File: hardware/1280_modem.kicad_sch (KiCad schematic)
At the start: 84 parts, among them IC1 SX1281IMLTRT, IC2 SKY65383-11, IC3 TJA1462AT_0Z, J2 Conn_Coaxial, J2 jst gh 4, J5 jst gh 6, J8 USB_C_Receptacle_USB2.0, J9 jst_sh 6, U13 STM32U575CGTx, U2 TPS7A20285PDBVR, U2 USBLC6-2SC6, U4 TPS7A2450DBVR, Y1 48MHz, Y1 52MHz

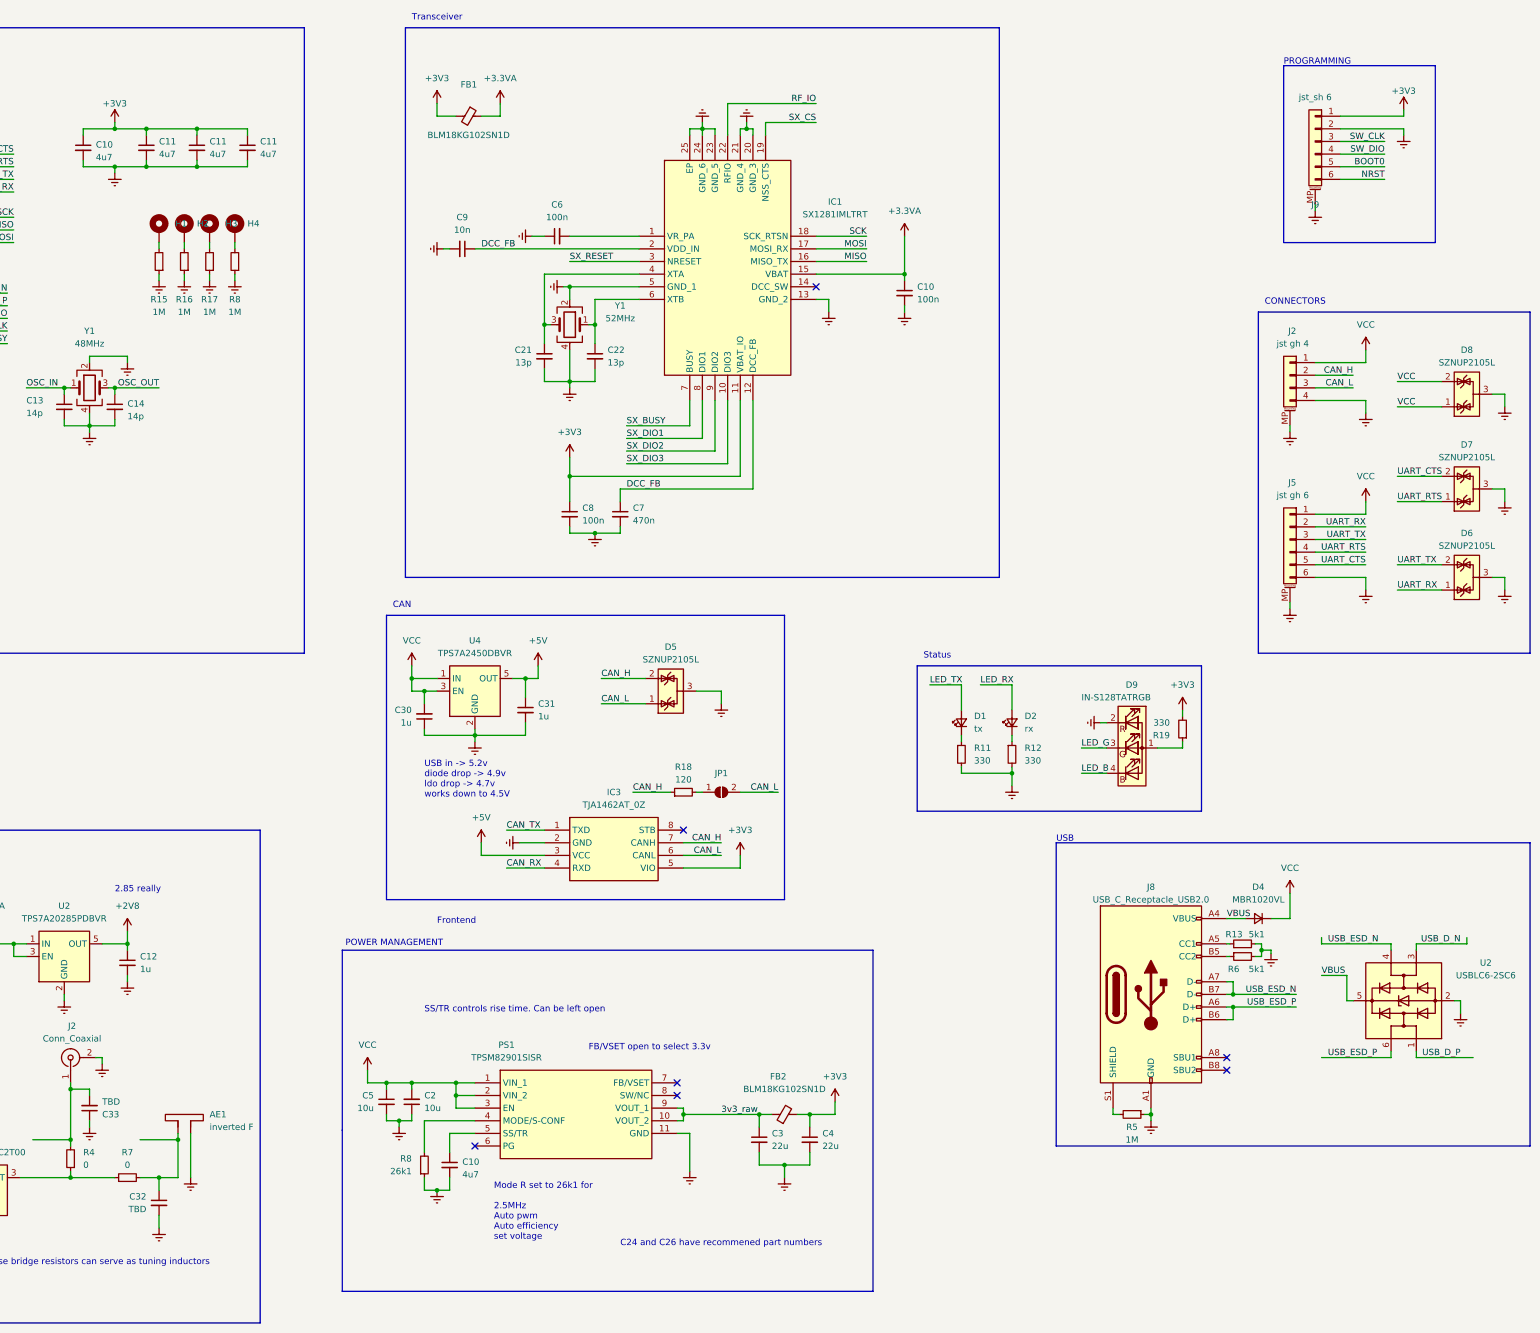
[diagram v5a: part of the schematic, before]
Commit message: better power electronics
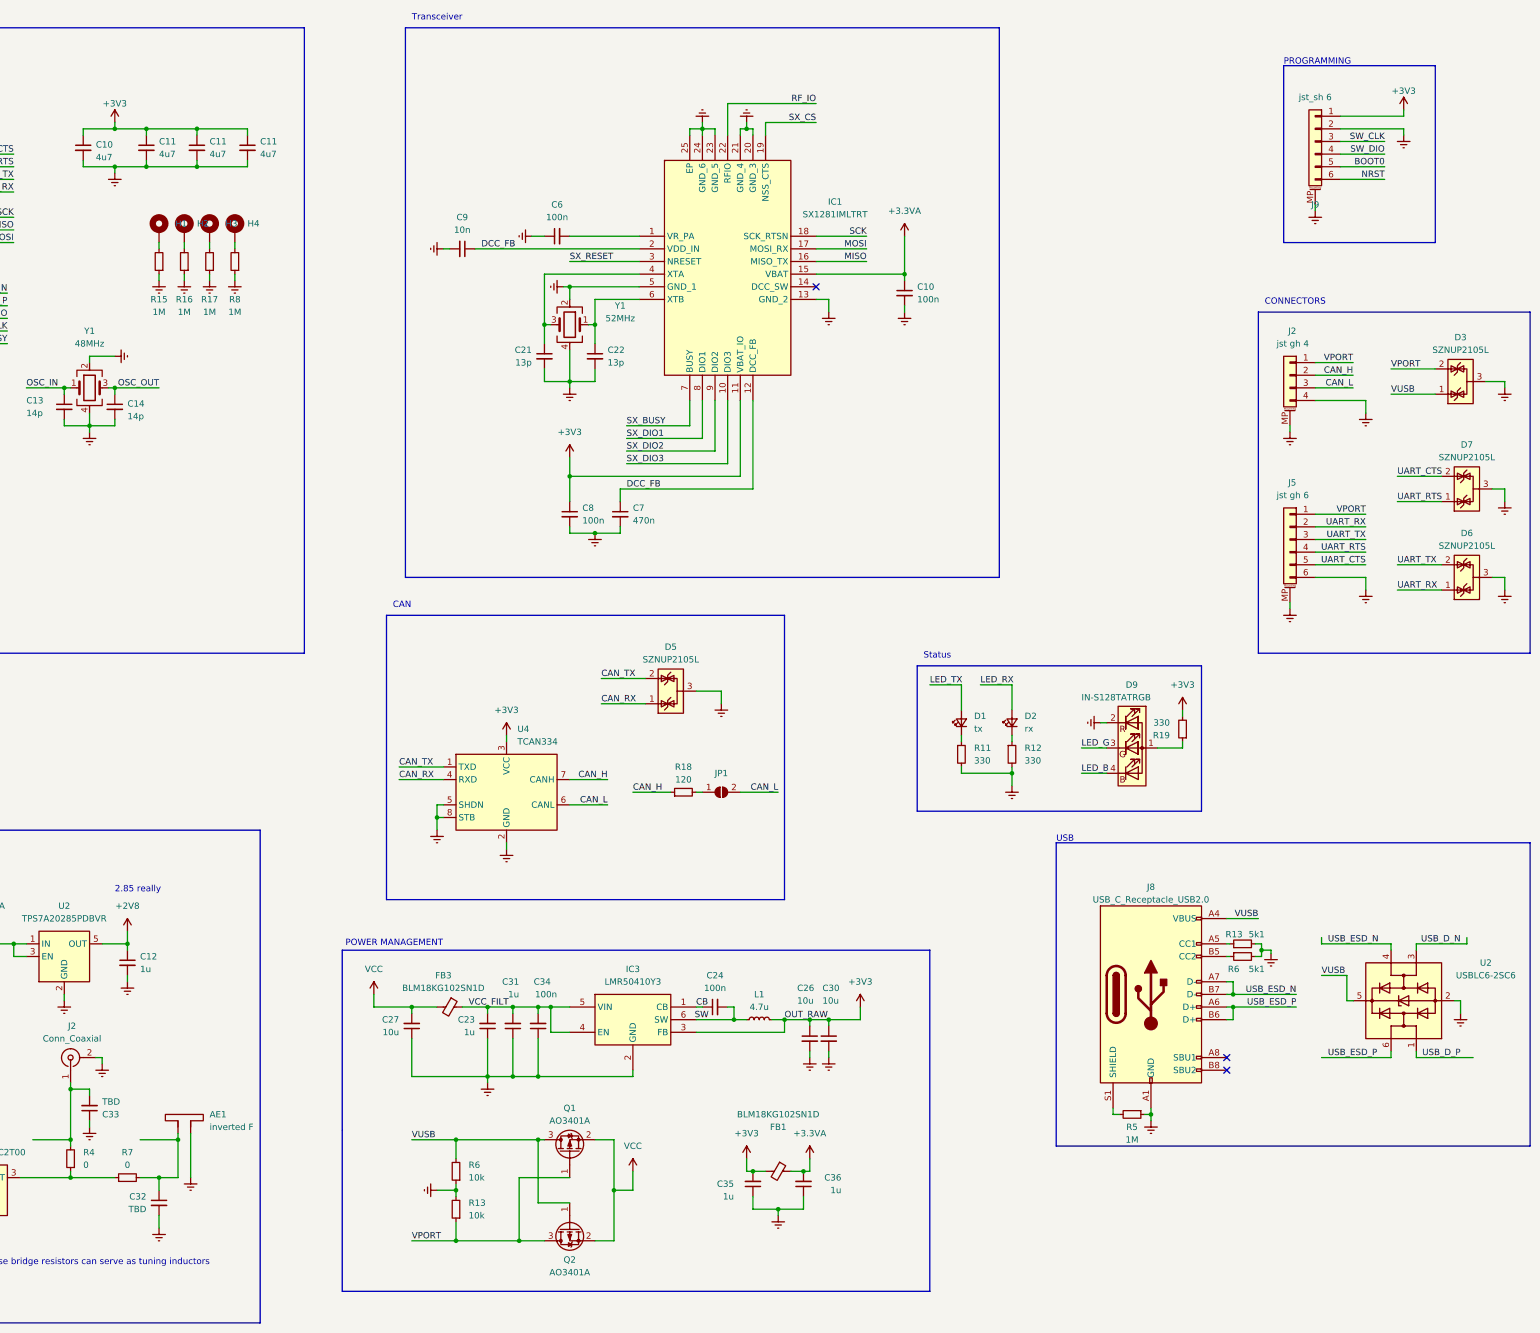
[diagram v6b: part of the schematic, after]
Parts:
- removed C10: 4u7, Capacitor_SMD:C_0603_1608Metric, symbol Device:C_Small
- removed C2, C5: 10u, Capacitor_SMD:C_1206_3216Metric, symbol Device:C_Small
- removed C3, C4: 22u, Capacitor_SMD:C_0805_2012Metric, symbol Device:C_Small
- removed D4: MBR1020VL, Diode_SMD:D_SOD-323_HandSoldering, symbol Device:D_Small
- removed D8: SZNUP2105L, Package_TO_SOT_SMD:SOT-23, symbol Power_Protection:SZNUP2105L
- removed FB2: BLM18KG102SN1D, Inductor_SMD:L_0805_2012Metric_Pad1.15x1.40mm_HandSolder, symbol Device:FerriteBead_Small
- removed IC3: TJA1462AT_0Z, tja1462:SOIC127P600X175-8N, symbol tja1462:TJA1462AT_0Z
- removed PS1: TPSM82901SISR, tpsm82901:TPSM82901SISR, symbol TPSM82901SISR:TPSM82901SISR
- removed R8: 26k1, Capacitor_SMD:C_0603_1608Metric, symbol Device:R_Small
- removed U4: TPS7A2450DBVR, Package_TO_SOT_SMD:SOT-23-5, symbol Regulator_Linear:TPS7A0525PDBV
- added C23, C35, C36: 1u, Capacitor_SMD:C_0603_1608Metric, symbol Device:C_Small
- added C24, C34: 100n, Capacitor_SMD:C_0603_1608Metric, symbol Device:C_Small
- added C26, C27: 10u, Capacitor_SMD:C_0603_1608Metric, symbol Device:C_Small
- added D3: SZNUP2105L, Package_TO_SOT_SMD:SOT-23, symbol Power_Protection:SZNUP2105L
- added FB3: BLM18KG102SN1D, Inductor_SMD:L_0805_2012Metric_Pad1.15x1.40mm_HandSolder, symbol Device:FerriteBead_Small
- added IC3: LMR50410Y3, lmr50410:SOT95P280X145-6N, symbol LMR50410YQDBVRQ1:LMR50410YQDBVRQ1
- added L1: 4.7u, Inductor_SMD_Wurth:L_Wurth_WE-LQSH-3012, symbol Device:L_Small
- added Q1, Q2: AO3401A, Package_TO_SOT_SMD:SOT-23, symbol Transistor_FET:AO3401A
- added R13, R6: 10k, Resistor_SMD:R_0603_1608Metric, symbol Device:R_Small
- added U4: TCAN334, Package_TO_SOT_SMD:TSOT-23-8, symbol Interface_CAN_LIN:TCAN334
- C30: value 1u -> 10u
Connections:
- net +5V is gone; now on net Earth: C31.1
- net +3.3VA: now also C36.2
- net +3V3: now also C30.1, C26.1, C35.2, IC3.3 (FB), L1.2, U4.3 (VCC)
- net CAN_H: now also U4.7 (CANH); no longer D5.2 (K)
- net CAN_L: now also U4.6 (CANL); no longer D5.1 (K)
- net CAN_RX: now also D5.1 (K), U4.4 (RXD)
- net CAN_TX: now also D5.2 (K), U4.1 (TXD)
- net Earth: now also C30.2, C23.1, C26.2, C27.1, C34.1, C35.1, C36.1, D3.3 (A), IC3.2 (GND), R13.2, R6.1, U4.2 (GND), U4.5 (SHDN), U4.8 (STB); no longer C30.1, C31.2
- net VCC: now also C27.2, FB3.2, Q1.2 (S), Q2.2 (S); no longer C30.2, J2.1 (Pin_1), J5.1 (Pin_1)
- net VBUS renamed VUSB
- net VUSB: now also D3.1 (K), Q1.3 (D), Q2.1 (G), R6.2
- new net CB: C24.1, IC3.1 (CB)
- new net SW: C24.2, IC3.6 (SW), L1.1
- new net VCC_FILT: C23.2, C31.2, C34.2, FB3.1, IC3.4 (EN), IC3.5 (VIN)
- new net VPORT: D3.2 (K), J2.1 (Pin_1), J5.1 (Pin_1), Q1.1 (G), Q2.3 (D), R13.1
- no-connect marks 14 -> 10
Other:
- note removed: "C24 and C26 have recommened part numbers"
- note removed: "FB/VSET open to select 3.3v"
- note removed: "Frontend"
- note removed: "Mode R set to 26k1 for 2.5MHz Auto pwm Auto efficiency set voltage"
- note removed: "SS/TR controls rise time. Can be left open"
- note removed: "USB in -> 5.2v diode drop -> 4.9v ldo drop -> 4.7v works down to 4.5V"
- moved on the sheet: FB1

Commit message: bamse
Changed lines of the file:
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@@
     (effects (font (size 1.27 1.27)) (justify right bottom))
   )
-  (label "VCC_FILT" (at 189.23 215.9 0) (fields_autoplaced)
+  (label "VCC_FILT" (at 187.96 215.9 0) (fields_autoplaced)
     (effects (font (size 1.27 1.27)) (justify left bottom))
   )

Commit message: second pass
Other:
- note added: "DIOs are generic interrupts"
- note added: "ok"
